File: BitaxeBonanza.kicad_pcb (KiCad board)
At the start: 6 copper layers, 76 x 87.5 mm, 260 parts, among them J1 XT30, J2 Conn_01x03, J4 Conn_01x04, J5 Conn_01x10, J6 USB_C_Receptacle_USB2.0, Q1 BSS138, SW3 SWITCH-SPST, SW4 SWITCH-SPST, U1 MCP1824T-1202E/OT, U11 RP2040, U12 ESP32-S3-WROOM-1, U13 TPS62933DRLR, U14 TPS62933DRLR, U15 STHW4-DU-HN050206, U16 STHW4-DU-HN050206, U17 STHW4-DU-HN050206, U2 TPS546D24SRVFR, U3 MCP1824T-1202E/OT, U4 MCP1824T-1202E/OT, U5 W25Q16JVUXIQ TR, U6 MCP1824T-1202E/OT, U8 SN74AXC4T774, U9 TPS22919DCKR, Y1 12MHz, Y2 50MHz

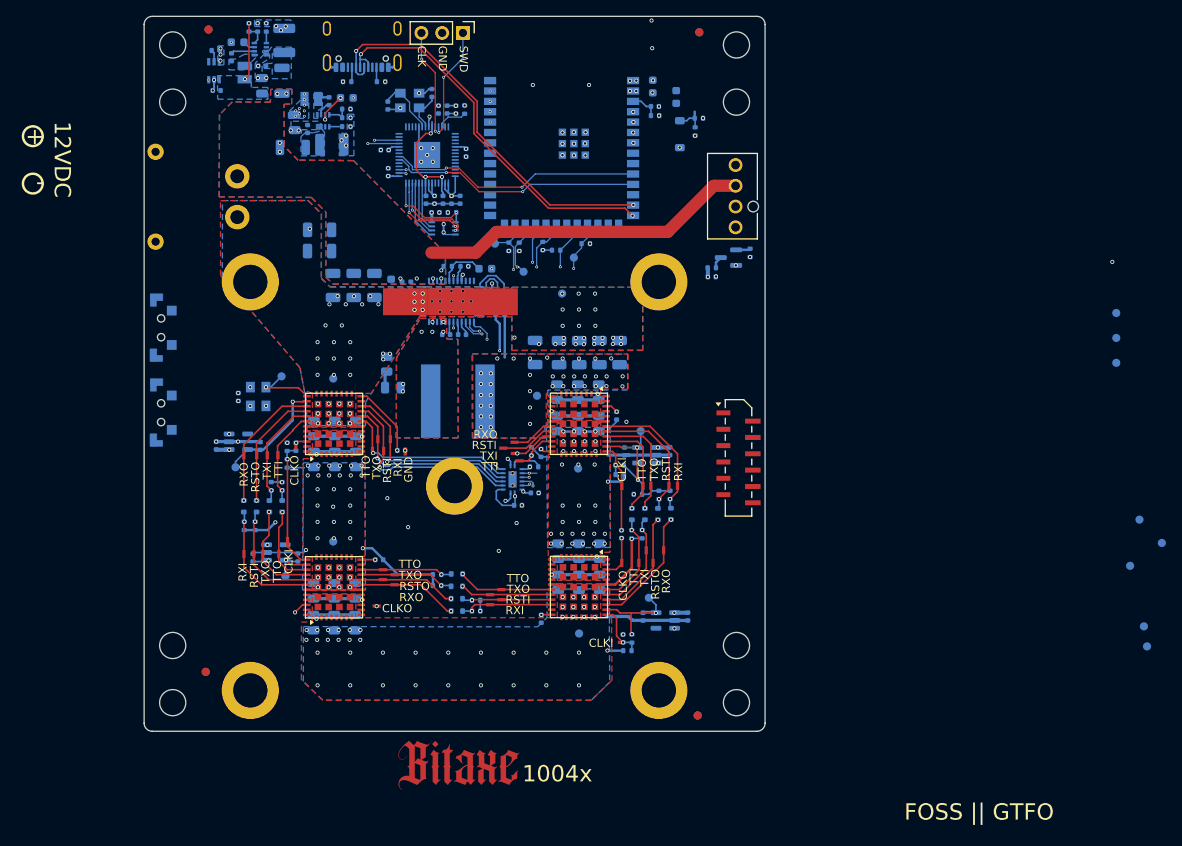
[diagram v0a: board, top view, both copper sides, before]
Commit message: switched display connector to BAP pins and UART instead of I2C. Bridge is now only ASIC serial. Added ESP32 ADC connections to domain midpoints.
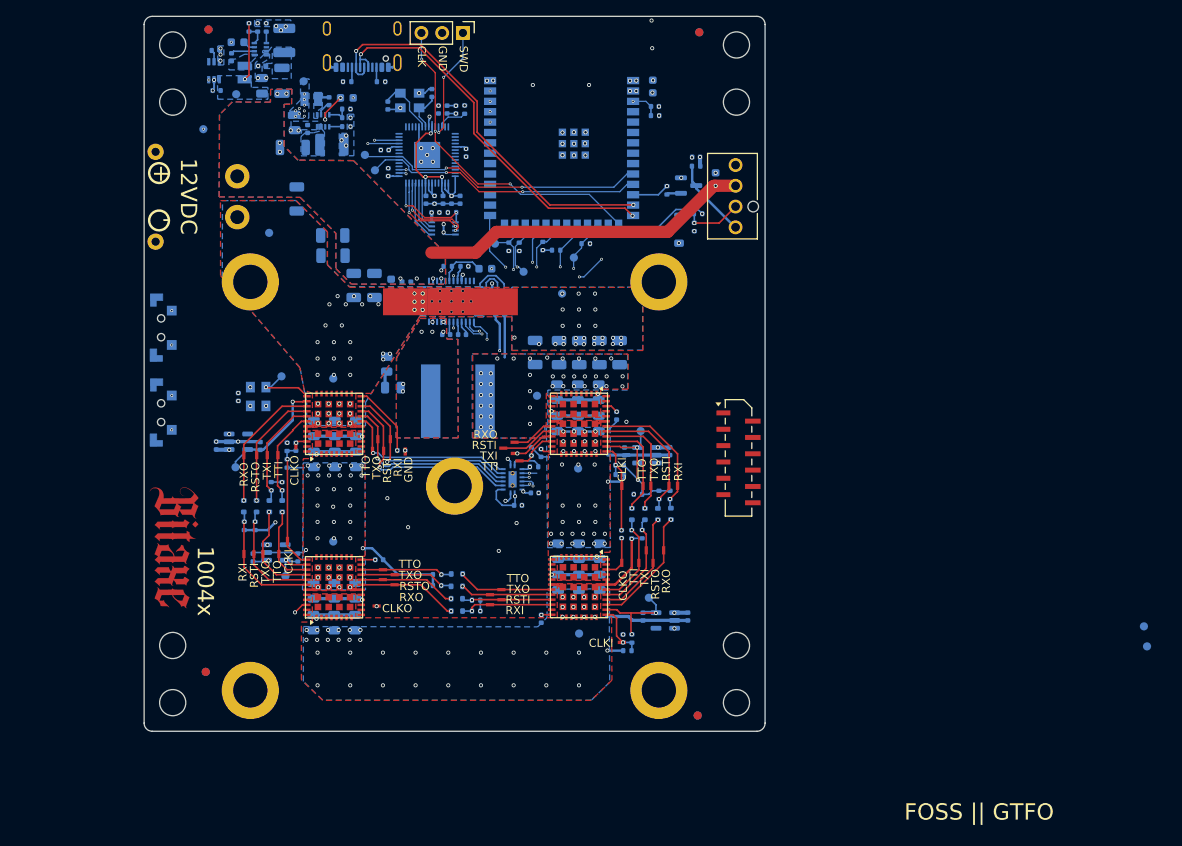
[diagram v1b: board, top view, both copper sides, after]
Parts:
- moved TP61 115.3 mm to (100.2, 68.3)
- moved TP26 113.0 mm to (108.3, 81.0)
- moved TP63 111.0 mm to (104.3, 64.0)
- moved TP25 106.6 mm to (121.2, 73.3)
- moved TP24 104.8 mm to (120.0, 71.5)
- moved TP62 104.3 mm to (112.5, 62.5)
- moved G*** 43.8 mm to (96.7, 119.5), turned to -90 degrees
- moved C77 14.8 mm to (160.6, 71.7), turned to 180 degrees
- moved R1 12.7 mm to (157.0, 75.8), turned to 90 degrees
- moved R34 12.6 mm to (160.6, 72.8), turned to 0 degrees
- moved D13 11.7 mm to (158.5, 80.6)
- moved R2 11.7 mm to (160.8, 78.7)
- moved R33 11.7 mm to (160.3, 80.3)
- moved C76 11.2 mm to (162.9, 74.4)
- moved Q1 10.1 mm to (159.6, 75.2), turned to 0 degrees
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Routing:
- net /Data/EN: track 3.57 -> 86.7 mm, vias 0 -> 4
- net /Data/IO0: track 0.00 -> 55.7 mm, vias 0 -> 2
- net /Data/SWCLK: track 13.3 -> 41.3 mm, vias 2 -> 3
- net /Data/FAN_TACH: track 0.06 -> 14.8 mm
- net /fan/FAN_PWM_PIN: track 1.57 -> 9.72 mm
- net /fan/FAN_TACH_PIN: track 3.90 -> 8.98 mm, vias 0 -> 1
- net /Data/FAN_PWM: track 0.01 -> 4.59 mm
- net /Data/ESP32_TX_DATA: track 31.3 -> 35.5 mm
- net /Data/ESP32_RX_DATA: track 30.9 -> 34.3 mm
- net /Data/SDA: vias 3 -> 2
- net GND: vias 141 -> 146
- net unconnected-(U12-GPIO7/TOUCH7/ADC1_CH6-Pad7): vias 1 -> 0
- net unconnected-(U12-GPIO6/TOUCH6/ADC1_CH5-Pad6): vias 1 -> 0
- net /Data/SWD-DISP: vias 1 -> 0
- net /Data/SWD-BRIDGE: vias 3 -> 2
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
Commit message: rough routing done.. DRC time
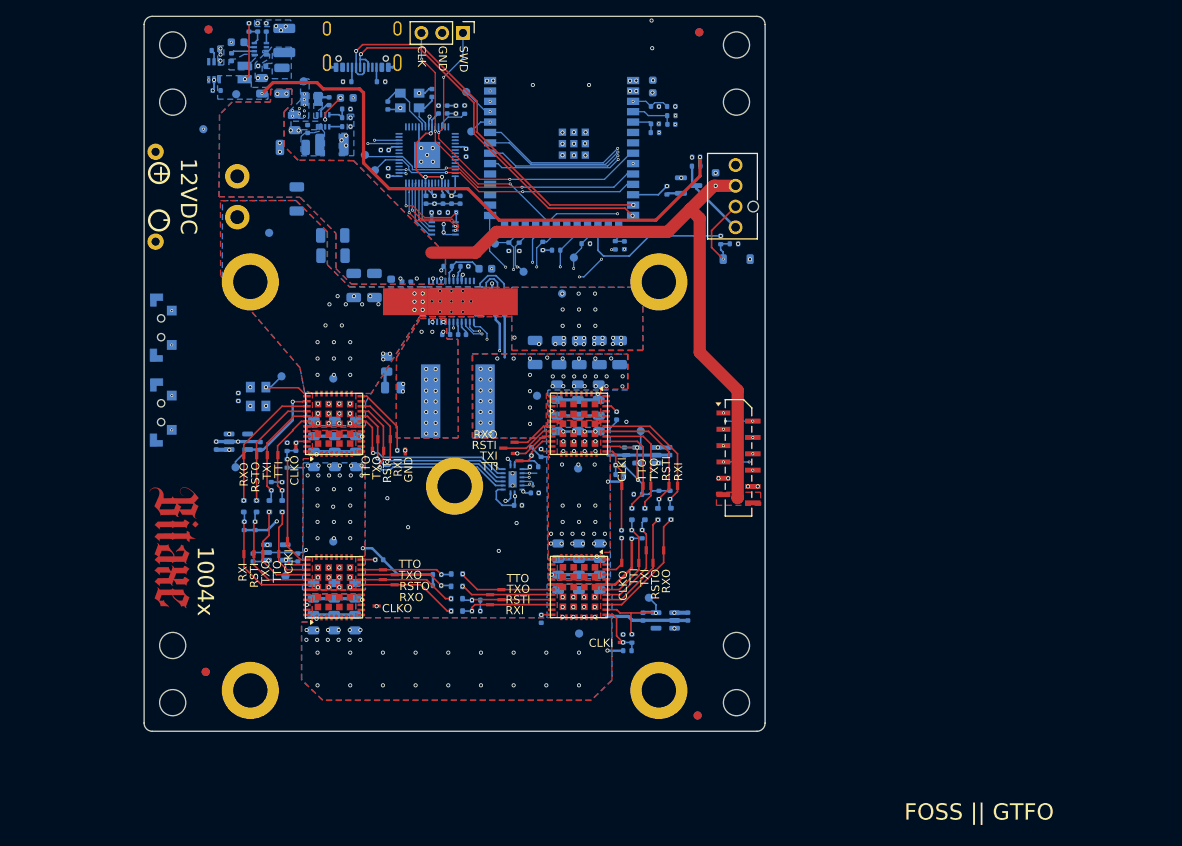
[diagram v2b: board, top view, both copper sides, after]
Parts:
- added C67: 0.1uF, Capacitor_SMD:C_0402_1005Metric, B.Cu at (151.8, 82.5)
- added C69: 0.1uF, Capacitor_SMD:C_0402_1005Metric, B.Cu at (157.5, 67.7)
- added C70: 0.1uF, Capacitor_SMD:C_0402_1005Metric, B.Cu at (155.5, 67.7)
- added R31: 5.1k, Resistor_SMD:R_0402_1005Metric, B.Cu at (150.7, 82.5)
- added R32: 5.1k, Resistor_SMD:R_0402_1005Metric, B.Cu at (157.5, 66.7)
- added R53: 5.1k, Resistor_SMD:R_0402_1005Metric, B.Cu at (155.5, 68.7)
- moved TP16 105.6 mm to (132.4, 63.8)
- moved TP23 104.0 mm to (133.0, 68.6)
- moved D13 7.92 mm to (165.5, 84.2), turned to 0 degrees
- moved R33 5.27 mm to (165.2, 82.3), turned to 0 degrees
- moved R2 4.25 mm to (163.6, 81.9), turned to 90 degrees
- moved R22 2.27 mm to (157.5, 65.5)
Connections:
- U12 pad 15: /Data/SWCLK -> Net-(U12-GPIO3/TOUCH3/ADC1_CH2*)
- U12 pad 22: unconnected-(U12-GPIO14/TOUCH14/ADC2_CH3/FSPIWP/FSPIDQS/SUBSPIWP-Pad22) -> /Data/SWCLK
- U12 pad 4: /Data/SWD-BRIDGE -> Net-(U12-GPIO4/TOUCH4/ADC1_CH3)
- U12 pad 5: /Data/SWD-DISP -> Net-(U12-GPIO5/TOUCH5/ADC1_CH4)
- U12 pad 8: unconnected-(U12-GPIO15/U0RTS/ADC2_CH4/XTAL_32K_P-Pad8) -> /Data/SWD-BRIDGE
- U12 pad 9: unconnected-(U12-GPIO16/U0CTS/ADC2_CH5/XTAL_32K_NH5-Pad9) -> /Data/SWD-DISP
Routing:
- net /ASIC/GND2: track 23.5 -> 122.4 mm, vias 38 -> 39
- net /ASIC/GND3: track 24.5 -> 112.6 mm, vias 44 -> 45
- net /5V: track 8.18 -> 78.9 mm, vias 3 -> 4
- net /Data/DISP_GPIO2: track 0.00 -> 67.5 mm, vias 0 -> 3
- net /Data/DISP_GPIO1: track 0.00 -> 66.3 mm, vias 0 -> 2
- net /Data/DISP_RX: track 0.00 -> 59.6 mm, vias 0 -> 2
- net /Data/DISP_TX: track 0.00 -> 59.0 mm, vias 0 -> 2
- net /ASIC/GND4: track 23.3 -> 72.9 mm, vias 34 -> 35
- net /Data/SWD-DISP: track 0.00 -> 39.8 mm, vias 0 -> 3
- net /12V: track 40.6 -> 78.4 mm
- net /3V3: track 39.3 -> 71.9 mm
- net /Data/SWCLK: track 41.3 -> 73.7 mm, vias 3 -> 5
- net /Data/SWD-BRIDGE: track 14.1 -> 42.0 mm, vias 2 -> 3
- net Net-(U12-GPIO4/TOUCH4/ADC1_CH3): track 0.00 -> 5.45 mm
- net /Data/FAN_TACH: track 14.8 -> 19.4 mm
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
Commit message: changed inductor to Bourns SRP1245A-1R2M as the coilcraft was out of stock everywhere.
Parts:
- D1, D10, D11, D12, D2, D3, D4, D5, D6, D7, D8, D9: value DLLFSD01T-7 -> BAS516
- J5: value Conn_01x10 -> Conn_01x12
- L1: footprint bitaxe:XAL1060122MEC -> bitaxe:SRP1245A-180M_BRN
- moved L1 1.55 mm to (132.7, 100.8)
- moved C24 0.44 mm to (141.3, 95.6)
- moved U17 0.14 mm to (136.1, 89.4)
- moved U15 0.14 mm to (124.8, 89.4)
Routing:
- net /ASIC/RX_1V2: track 24.2 -> 31.1 mm
- net /ASIC/TX_1V2: track 23.3 -> 29.2 mm
- net /ASIC/RST_1V2: track 25.0 -> 30.2 mm
- net /ASIC/TRIP_3V3: track 101.1 -> 100.2 mm
- net /Data/EN: track 88.5 -> 87.9 mm
- net GND: vias 155 -> 188
- net /VDD: vias 40 -> 54
- net /Power/SW1: vias 21 -> 82
- net /Data/FAN_PWM: vias 1 -> 0
- net /12V: vias 10 -> 45

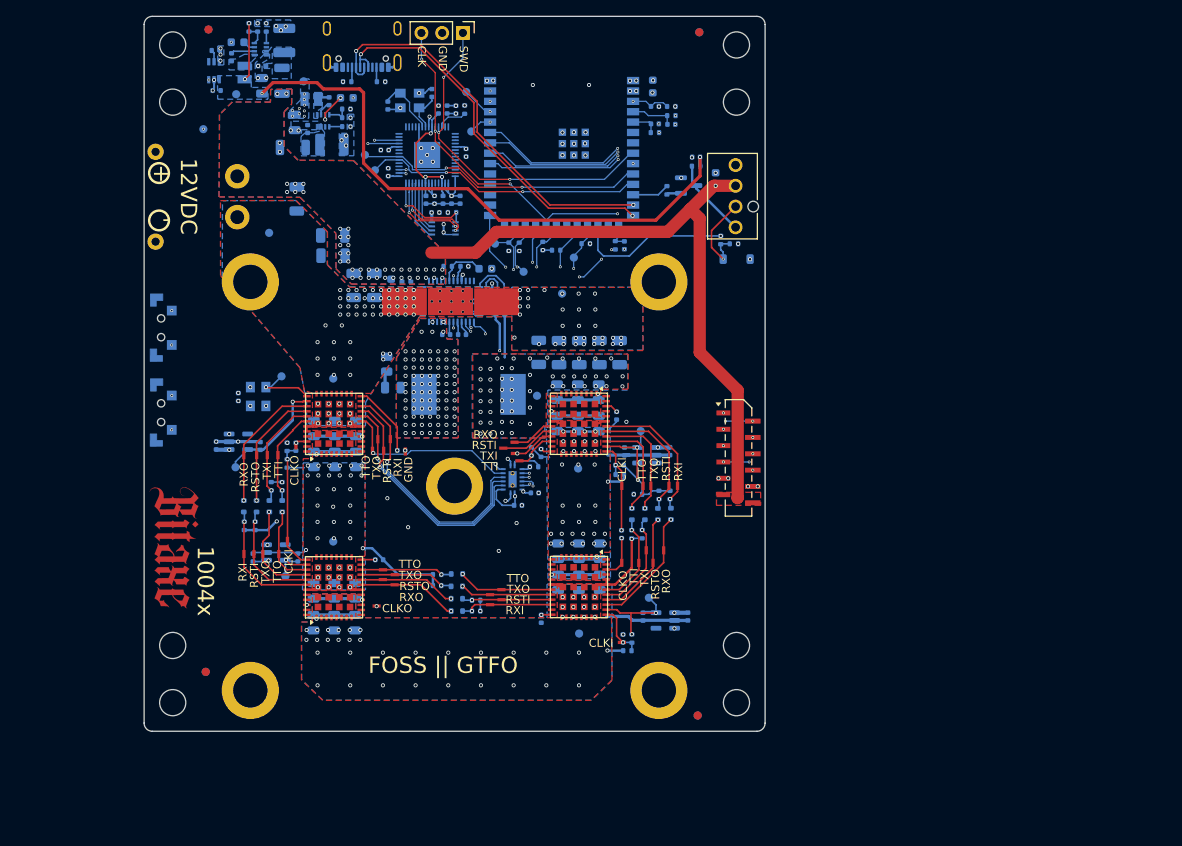
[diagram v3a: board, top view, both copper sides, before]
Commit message: added stitching vias. added test points for ASIC signals pre-level shifter
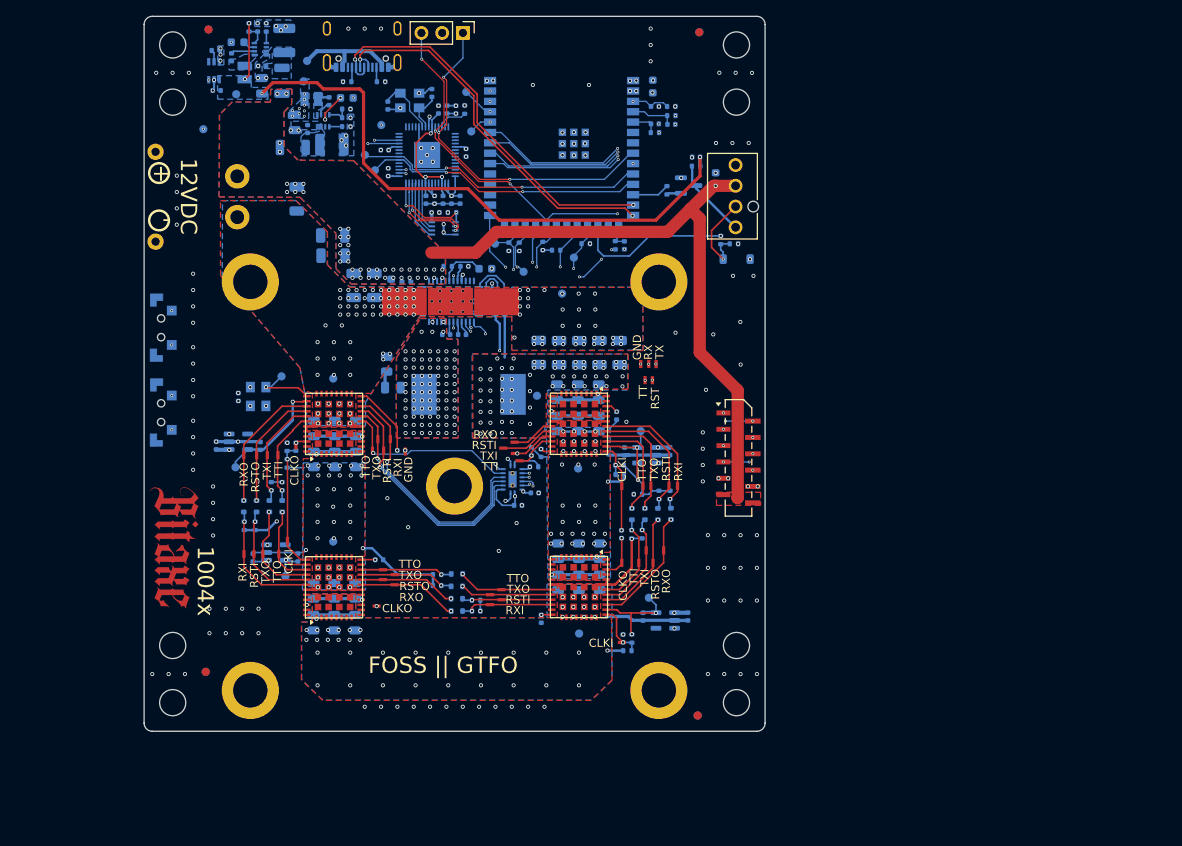
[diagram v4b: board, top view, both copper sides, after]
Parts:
- added TP64: VBUS, bitaxe:TestPoint_Pad_D1.0mm, B.Cu at (112.9, 60.0)
- added TP65: TX, bitaxe:TestPoint_Pad_1.0x0.4mm, F.Cu at (155.7, 97.1)
- added TP66: RX, bitaxe:TestPoint_Pad_1.0x0.4mm, F.Cu at (154.8, 97.0)
- added TP67: TT, bitaxe:TestPoint_Pad_1.0x0.4mm, F.Cu at (154.3, 99.0)
- added TP68: RST, bitaxe:TestPoint_Pad_1.0x0.4mm, F.Cu at (155.2, 99.0)
- added TP69: GND, bitaxe:TestPoint_Pad_1.0x0.4mm, F.Cu at (153.8, 97.0)
- moved TP26 19.0 mm to (122.0, 67.8)
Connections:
- J6 pad A4: unconnected-(J6-VBUS-PadA4)_1 -> Net-(J6-VBUS-PadA4)
- J6 pad B4: unconnected-(J6-VBUS-PadA4) -> Net-(J6-VBUS-PadA4)
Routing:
- net Net-(J6-VBUS-PadA4): track 0.00 -> 12.8 mm
- net /Data/SWCLK: track 73.9 -> 74.6 mm
- net /ASIC/TX_3V3: track 82.5 -> 83.1 mm, vias 2 -> 3
- net /ASIC/GND3: track 112.4 -> 112.9 mm
- net /ASIC/GND2: track 122.0 -> 122.5 mm
- net /ASIC/RST_3V3: track 98.8 -> 99.2 mm, vias 2 -> 3
- net /ASIC/RX_3V3: track 81.4 -> 81.6 mm, vias 2 -> 3
- net GND: vias 188 -> 279
- net /VDD: vias 54 -> 68
- net /ASIC/TRIP_3V3: vias 2 -> 3
